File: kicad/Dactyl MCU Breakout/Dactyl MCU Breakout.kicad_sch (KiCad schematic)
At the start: 23 parts, among them J1 Columns, J2 Rows, J3 Thumbs, J4 Display, J5 Split, J6 Extrernal, J7 JST, SW1 Reset, SW2 Battery, SW3 LED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

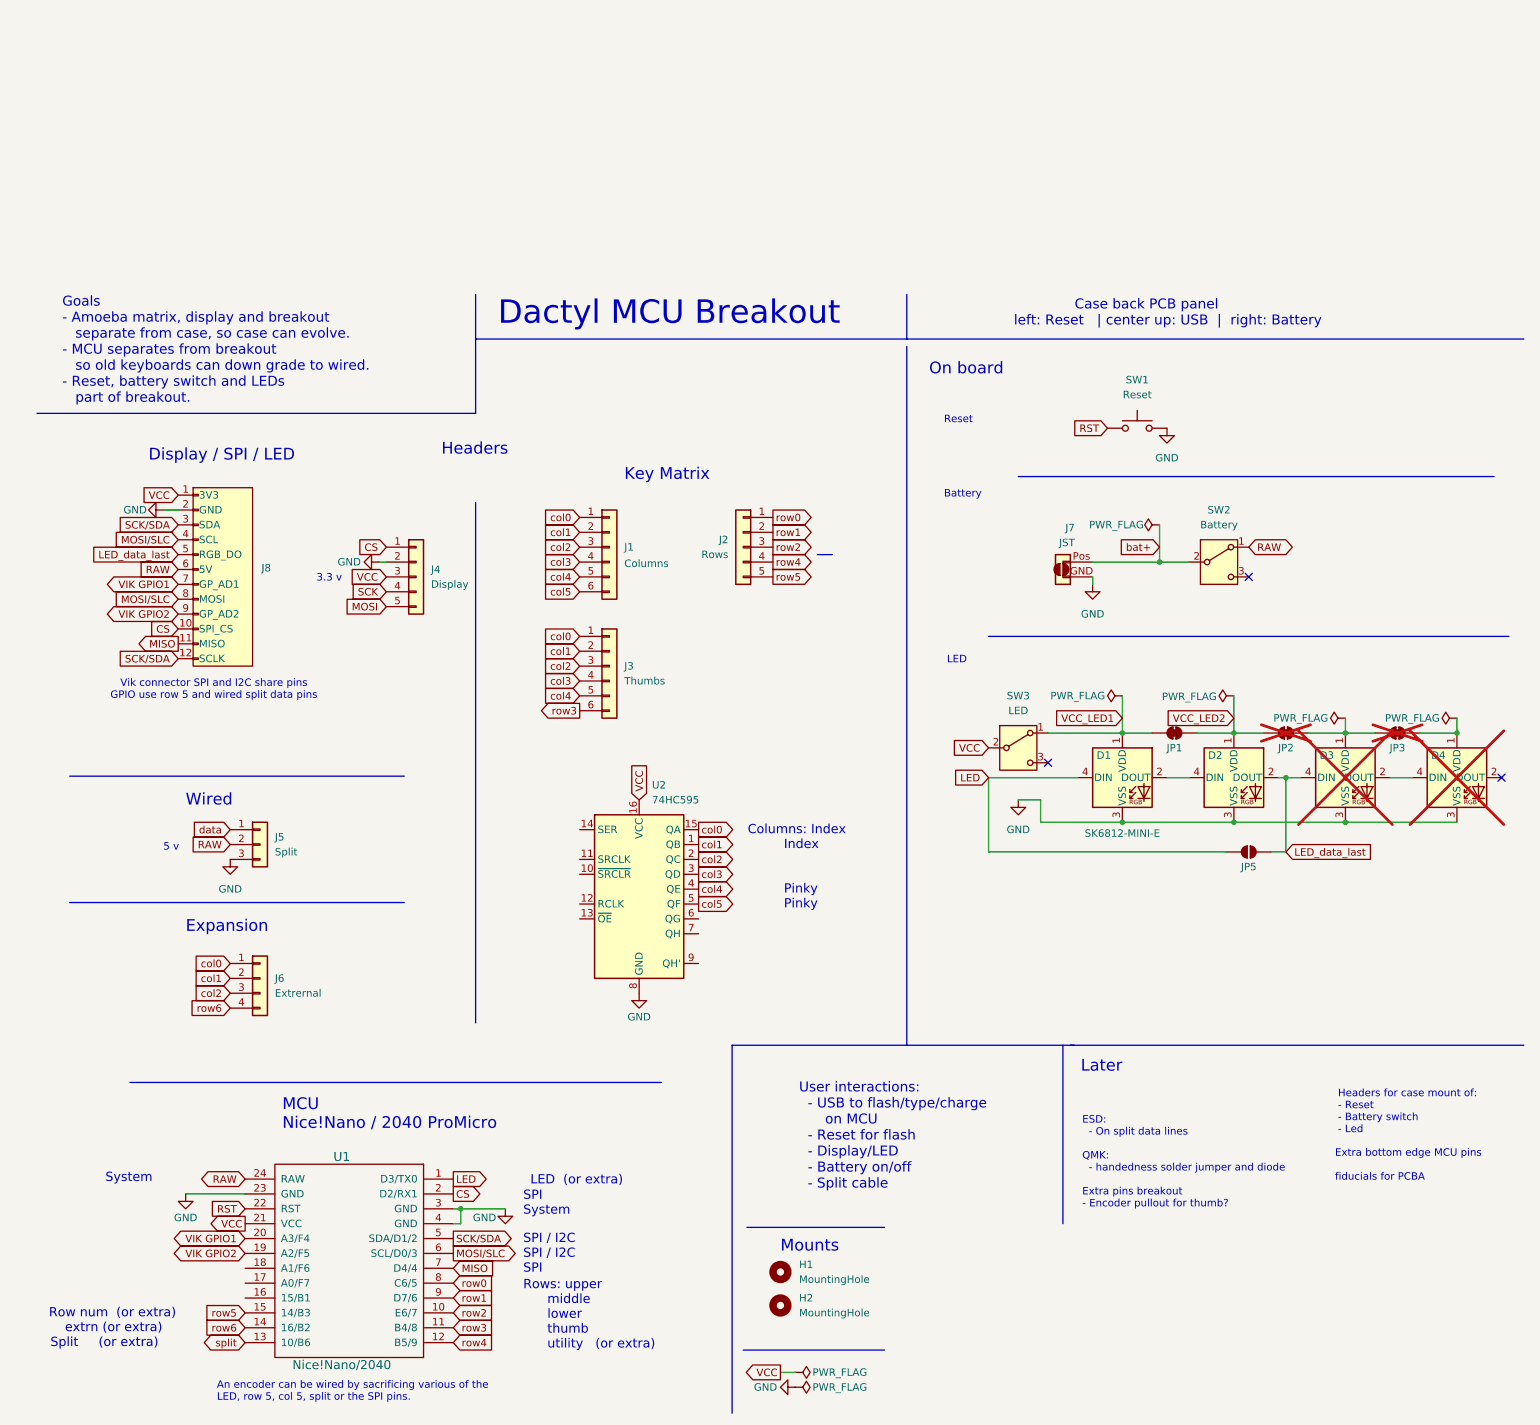
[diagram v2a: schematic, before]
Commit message: refactor: half sheet schematic, for non-reversable
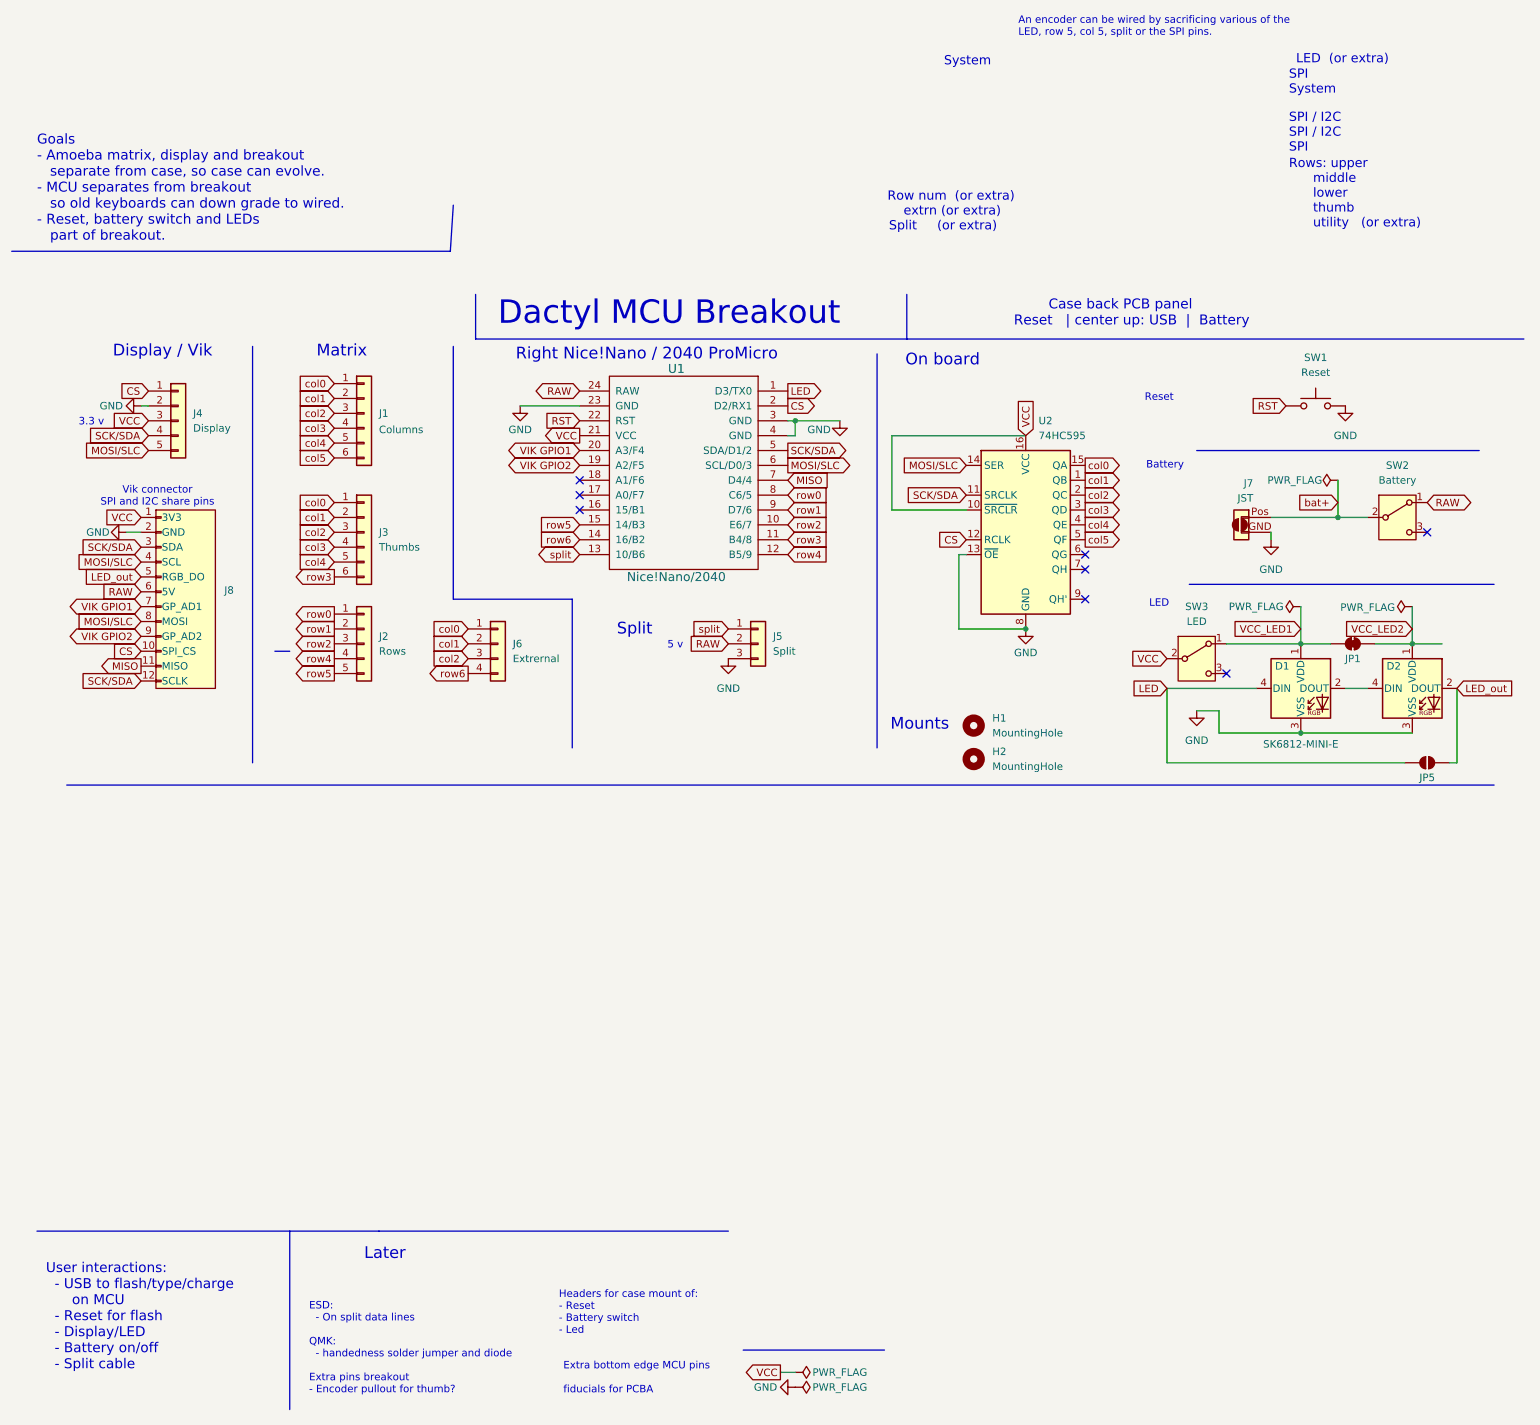
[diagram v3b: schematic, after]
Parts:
- removed D3, D4: SK6812-MINI-E, Dactyl:SK6812-MINI-E-Dog2, symbol Dactyl:SK6812-MINI-E
- removed JP2: LED3 cutoff, Jumper:SolderJumper-2_P1.3mm_Bridged_RoundedPad1.0x1.5mm, symbol Jumper:SolderJumper_2_Bridged
- removed JP3: LED4 cutoff, Jumper:SolderJumper-2_P1.3mm_Bridged_RoundedPad1.0x1.5mm, symbol Jumper:SolderJumper_2_Bridged
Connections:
- net MOSI is gone; now on net MOSI/SLC: J4.5 (Pin_5)
- net SCK is gone; now on net SCK/SDA: J4.4 (Pin_4)
- net data is gone; now on net split: J5.1 (Pin_1)
- net CS: now also U2.12 (RCLK)
- net GND: now also U2.13 (~{OE})
- net MOSI/SLC: now also U2.14 (SER)
- net SCK/SDA: now also U2.11 (SRCLK)
- net VCC: now also U2.10 (~{SRCLR})
- net LED_data_last renamed LED_out
- no-connect marks 3 -> 8
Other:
- note added: "Case back PCB panel Reset | center up: USB | Battery"
- note added: "Display / Vik"
- note added: "Matrix"
- note added: "Right Nice!Nano / 2040 ProMicro"
- note added: "Split"
- note added: "Vik connector SPI and I2C share pins"
- note removed: "Case back PCB panel left: Reset | center up: USB | right: Battery"
- note removed: "Columns: Index Index Pinky Pinky"
- note removed: "Display / SPI / LED"
- note removed: "Expansion"
- note removed: "Headers"
- note removed: "Key Matrix"
- note removed: "MCU Nice!Nano / 2040 ProMicro"
- note removed: "Vik connector SPI and I2C share pins GPIO use row 5 and wired split data pins"
- note removed: "Wired"
- moved on the sheet: D1, D2, H1, H2, J1, J2, J3, J4, J5, J6, J7, J8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
